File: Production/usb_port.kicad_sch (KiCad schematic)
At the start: 85 parts, among them J401 TYPE-C 16PCB1.6 IP68, Q401 PGQ04N070, Q402 PGQ04N070, Q407 PGQ04N070, Q408 PGQ04N070, U401 TPS25751DREFR, U402 M24512-DFMC6TG, U403 BQ25756RRVR, U404 TPS62933DRLR, U405 TPD4S201TRGRRQ1

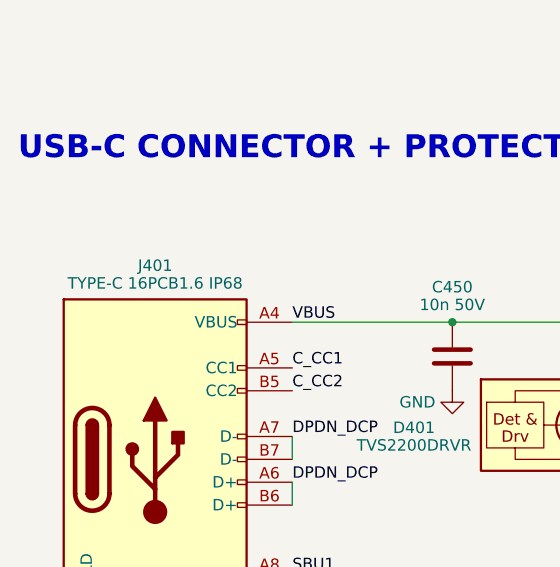
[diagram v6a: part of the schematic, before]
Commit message: Production board: 6-layer 0.8 mm stack-up, top-cap outline, pour plan
tools/make_board.py patches Monolith.kicad_pcb (footprints untouched): 6 layers,
0.8 mm, 2 oz outer / 0.5 oz inner, ENIG, filled vias; 40.5 mm R9.35 outline
from mechanical/monolith_parts.py (the bottom DXF is the end board). Via
minimum 0.35/0.2 for fan-out. J401/J501 -> TYPE-C 16PCB0.8 IP68 (C55629727).
Pour plan in Production/README.md.

Co-Authored-By: Claude Opus 5.5 <noreply@anthropic.com>
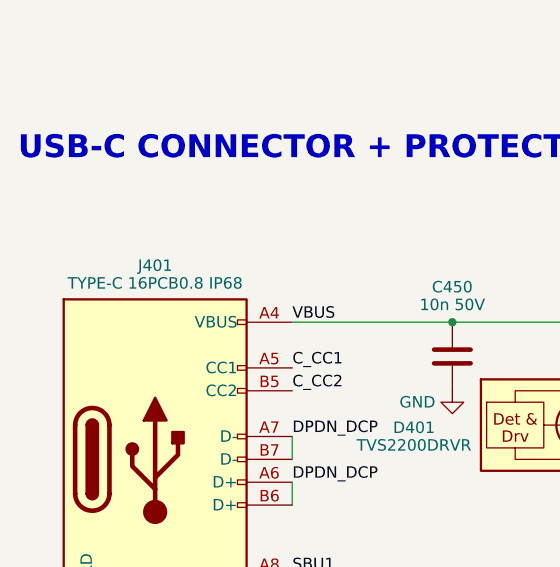
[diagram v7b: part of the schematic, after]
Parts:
- J401: value TYPE-C 16PCB1.6 IP68 -> TYPE-C 16PCB0.8 IP68; footprint MonolithDev:USB_C_Receptacle_ShouHan_TYPE-C_16PCB1.6_IP68 -> MonolithDev:USB_C_Receptacle_ShouHan_TYPE-C_16PCB0.8_IP68; LCSC C55629729 -> C55629727; MPN TYPE-C 16PCB1.6 IP68 (Shou Han) -> TYPE-C 16PCB0.8 IP68 (Shou Han)
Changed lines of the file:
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@@
 			)
 		)
-		(property "Value" "TYPE-C 16PCB1.6 IP68"
+		(property "Value" "TYPE-C 16PCB0.8 IP68"
 			(at 45.72 76.96 0)
 			(show_name no)
@@
 			)
 		)
-		(property "Footprint" "MonolithDev:USB_C_Receptacle_ShouHan_TYPE-C_16PCB1.6_IP68"
+		(property "Footprint" "MonolithDev:USB_C_Receptacle_ShouHan_TYPE-C_16PCB0.8_IP68"
 			(at 49.53 96.52 0)
 			(hide yes)
@@
 			)
 		)
-		(property "LCSC" "C55629729"
+		(property "LCSC" "C55629727"
 			(at 45.72 96.52 0)
 			(hide yes)
@@
 			)
 		)
-		(property "MPN" "TYPE-C 16PCB1.6 IP68 (Shou Han)"
+		(property "MPN" "TYPE-C 16PCB0.8 IP68 (Shou Han)"
 			(at 45.72 96.52 0)
 			(hide yes)

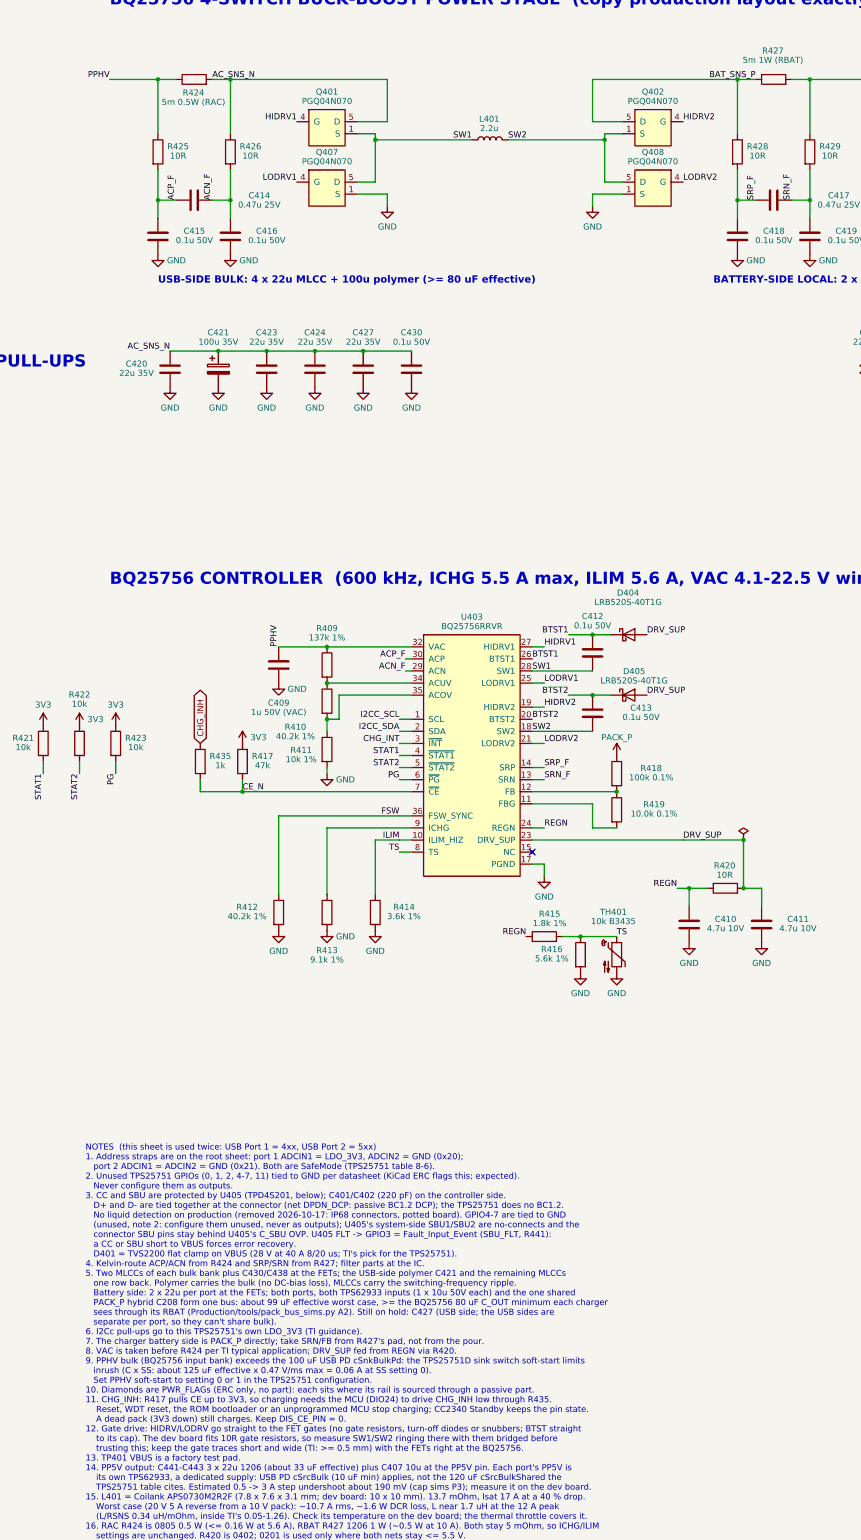
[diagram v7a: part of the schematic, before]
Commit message: Production schematic P0: one Vishay SiZ240DT half-bridge per charger leg
Q401+Q407 -> Q401 (SiZ240DT units A/B), Q402+Q408 -> Q402, both ports; new
2-unit symbol with the old FET pin geometry (no wires moved) and the PowerPAIR
3x3S footprint from Vishay's land pattern (doc 78115), in tools/siz240dt.py.
check_netlist maps old FET pins to the new units: nets unchanged. Courtyard
1981 -> 1923 mm2. ERC: expected warnings only.

Co-Authored-By: Claude Opus 5.5 <noreply@anthropic.com>
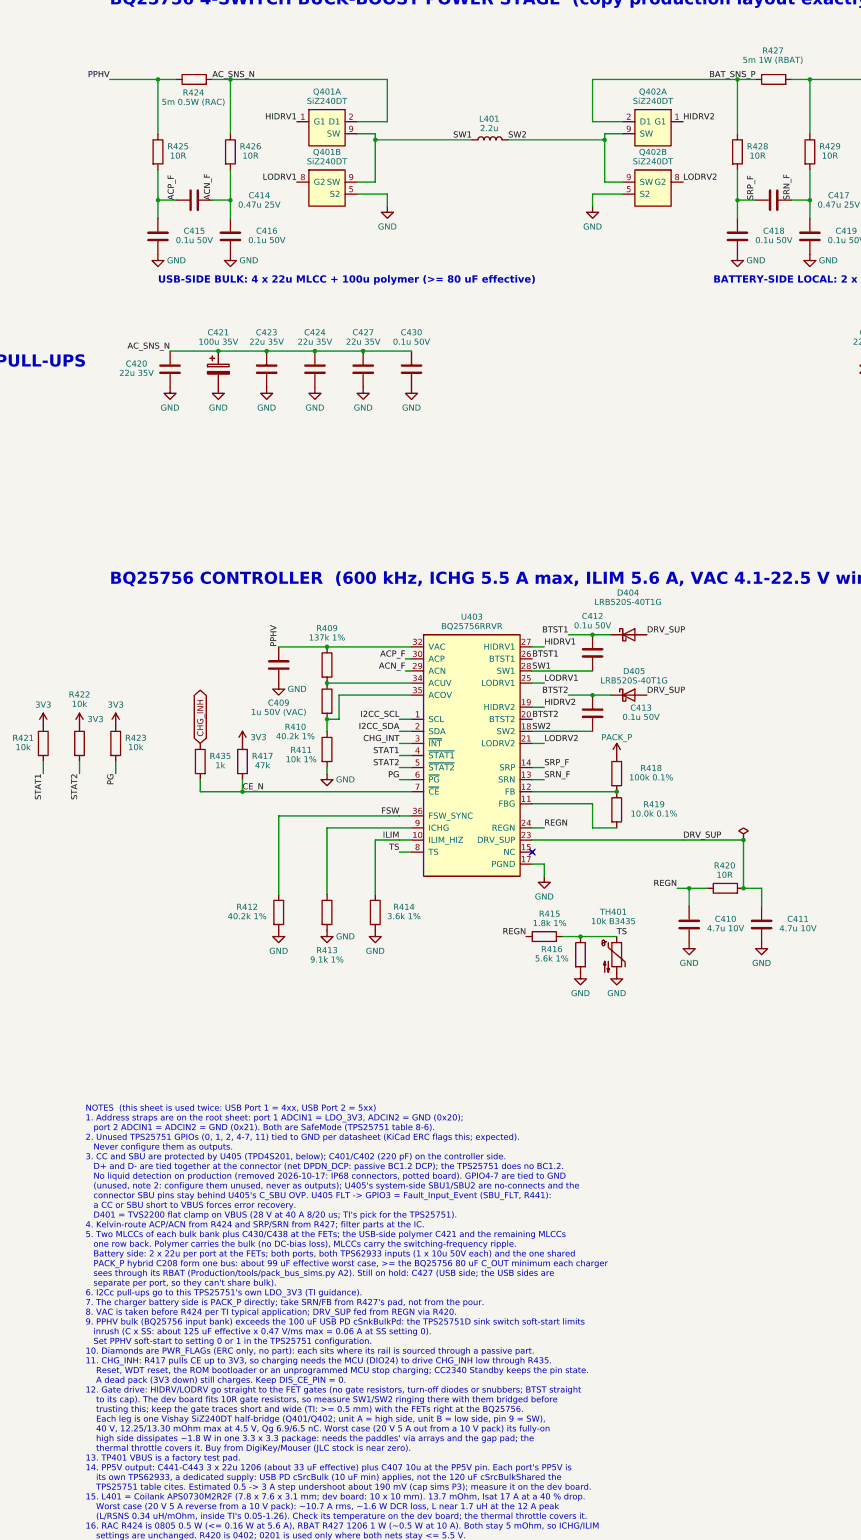
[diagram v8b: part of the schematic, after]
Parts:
- Q401: renamed from Q407; value PGQ04N070 -> SiZ240DT; footprint MonolithDev:AGM_PDFN-8_3.3x3.3mm_P0.65mm -> MonolithDev:Vishay_PowerPAIR_3x3S; symbol MonolithDev:PGQ04N070 -> MonolithDev:SiZ240DT; LCSC C49384056 -> C3289403; MPN PGQ04N070 (JinYu) -> SiZ240DT-T1-GE3 (Vishay)
- Q401, Q402: value PGQ04N070 -> SiZ240DT; footprint MonolithDev:AGM_PDFN-8_3.3x3.3mm_P0.65mm -> MonolithDev:Vishay_PowerPAIR_3x3S; symbol MonolithDev:PGQ04N070 -> MonolithDev:SiZ240DT; LCSC C49384056 -> C3289403; MPN PGQ04N070 (JinYu) -> SiZ240DT-T1-GE3 (Vishay)
- Q402: renamed from Q408; value PGQ04N070 -> SiZ240DT; footprint MonolithDev:AGM_PDFN-8_3.3x3.3mm_P0.65mm -> MonolithDev:Vishay_PowerPAIR_3x3S; symbol MonolithDev:PGQ04N070 -> MonolithDev:SiZ240DT; LCSC C49384056 -> C3289403; MPN PGQ04N070 (JinYu) -> SiZ240DT-T1-GE3 (Vishay)
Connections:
- net AC_SNS_N: now also Q401.2 (D1), Q401.3 (D1), Q401.4 (D1); no longer Q401.5 (D), Q401.6 (D), Q401.7 (D), Q401.8 (D)
- net BAT_SNS_P: now also Q402.2 (D1), Q402.3 (D1), Q402.4 (D1); no longer Q402.5 (D), Q402.6 (D), Q402.7 (D), Q402.8 (D)
- net GND: now also Q401.5 (S2), Q401.6 (S2), Q401.7 (S2), Q402.5 (S2), Q402.6 (S2), Q402.7 (S2); no longer Q401.1 (S), Q401.2 (S), Q401.3 (S), Q402.1 (S), Q402.2 (S), Q402.3 (S)
- net HIDRV1: now also Q401.1 (G1); no longer Q401.4 (G)
- net HIDRV2: now also Q402.1 (G1); no longer Q402.4 (G)
- net LODRV1: now also Q401.8 (G2); no longer Q401.4 (G)
- net LODRV2: now also Q402.8 (G2); no longer Q402.4 (G)
- net SW1: now also Q401.9 (SW), Q401.9 (SW); no longer Q401.1 (S), Q401.2 (S), Q401.3 (S), Q401.5 (D), Q401.6 (D), Q401.7 (D), Q401.8 (D)
- net SW2: now also Q402.9 (SW), Q402.9 (SW); no longer Q402.1 (S), Q402.2 (S), Q402.3 (S), Q402.5 (D), Q402.6 (D), Q402.7 (D), Q402.8 (D)
